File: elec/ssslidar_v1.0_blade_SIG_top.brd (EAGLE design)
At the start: 12.5 x 7 mm, 31 parts, among them P1 PIN_SMD_0.8X1_RECT, P10 PIN_SMD_0.8X1_RECT, P11 PIN_SMD_1X1_RECT, P12 PIN_SMD_0.8X1_RECT, P13 PIN_SMD_0.8X1_RECT, P14 PIN_SMD_0.8X1_RECT, P15 PIN_SMD_0.8X1_RECT, P16 PIN_SMD_0.8X1_RECT, P17 PIN_SMD_1X1_RECT, P18 PIN_SMD_0.8X1_RECT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

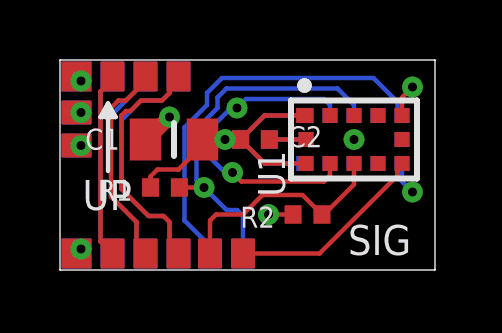
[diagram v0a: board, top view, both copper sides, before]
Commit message: Upadted blade footprint, put everything in v1.0
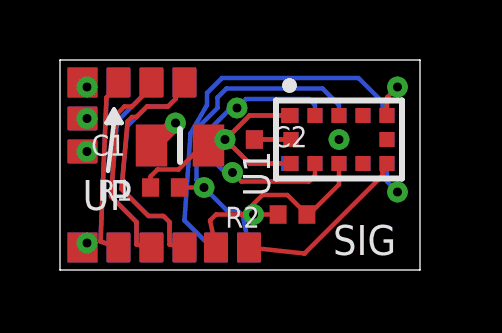
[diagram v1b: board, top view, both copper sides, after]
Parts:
- moved C2 0.50 mm to (6.00, 4.35)
- moved C3 0.50 mm to (6.00, 4.35)
- moved R2 0.50 mm to (7.75, 1.85)
- moved U1 0.50 mm to (9.30, 4.35)
- moved U2 0.50 mm to (9.30, 4.35)
- moved P1 0.28 mm to (4.15, 6.25)
- moved P22 0.28 mm to (4.15, 6.25)
- moved P10 0.28 mm to (0.75, 5.05)
- moved P12 0.28 mm to (0.75, 5.05)
- moved P13 0.28 mm to (0.75, 3.95)
- moved P14 0.28 mm to (1.95, 6.25)
- moved P16 0.28 mm to (0.75, 3.95)
- moved P18 0.28 mm to (4.15, 0.75)
- moved P19 0.28 mm to (4.15, 0.75)
- moved P2 0.28 mm to (0.75, 6.25)
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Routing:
- net SCL: track 16.6 -> 15.4 mm
- net VDD: track 17.8 -> 16.7 mm
- net SDA1: track 8.06 -> 7.10 mm
- net INT2: track 13.4 -> 12.7 mm
- net INT1: track 6.69 -> 6.00 mm
- net SDA2: track 12.6 -> 11.9 mm
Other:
- board size 12.5 x 7 mm -> 12 x 7 mm
